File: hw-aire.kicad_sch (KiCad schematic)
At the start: 59 parts, among them J1 Conn_01x02_Pin, J3 Screw_Terminal_01x12, J4 Conn_01x05_Pin, J5 Conn_01x02_Pin, K1 JRC-21F(4100), K2 JRC-21F(4100), K3 JRC-21F(4100), Q1 PMBT3904235, Q2 PMBT3904235, Q3 PMBT3904235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

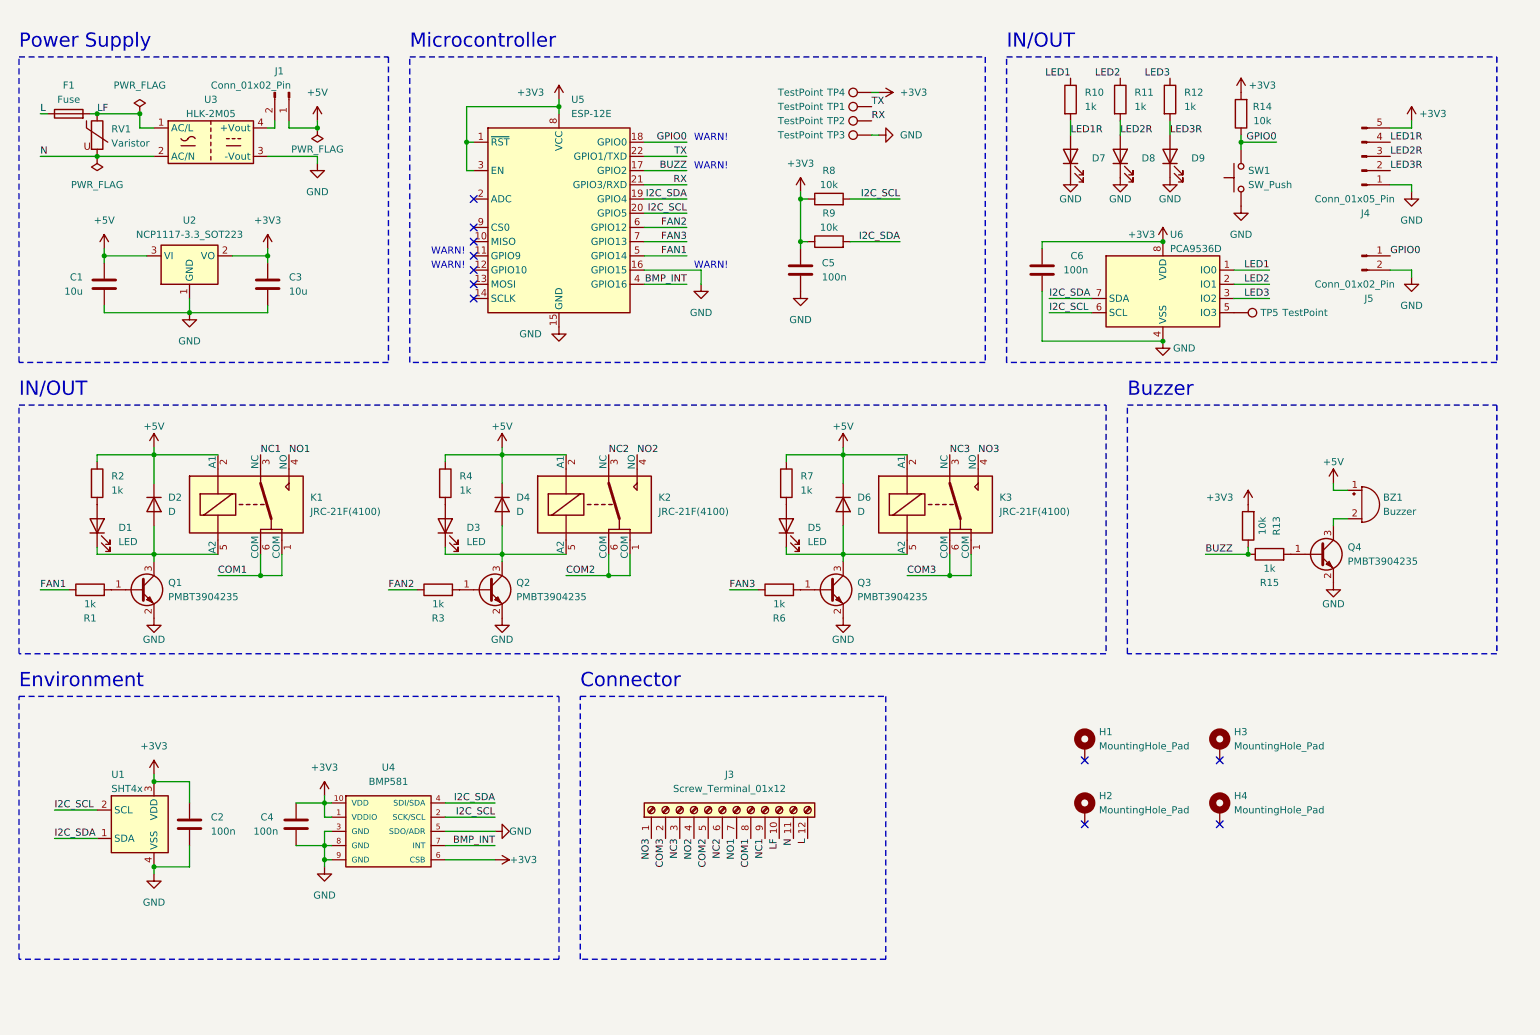
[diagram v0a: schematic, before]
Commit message: Start changing SCH for rev 3.0
- Change ESP8266 to ESP32-SOLO
- Change to cold relays
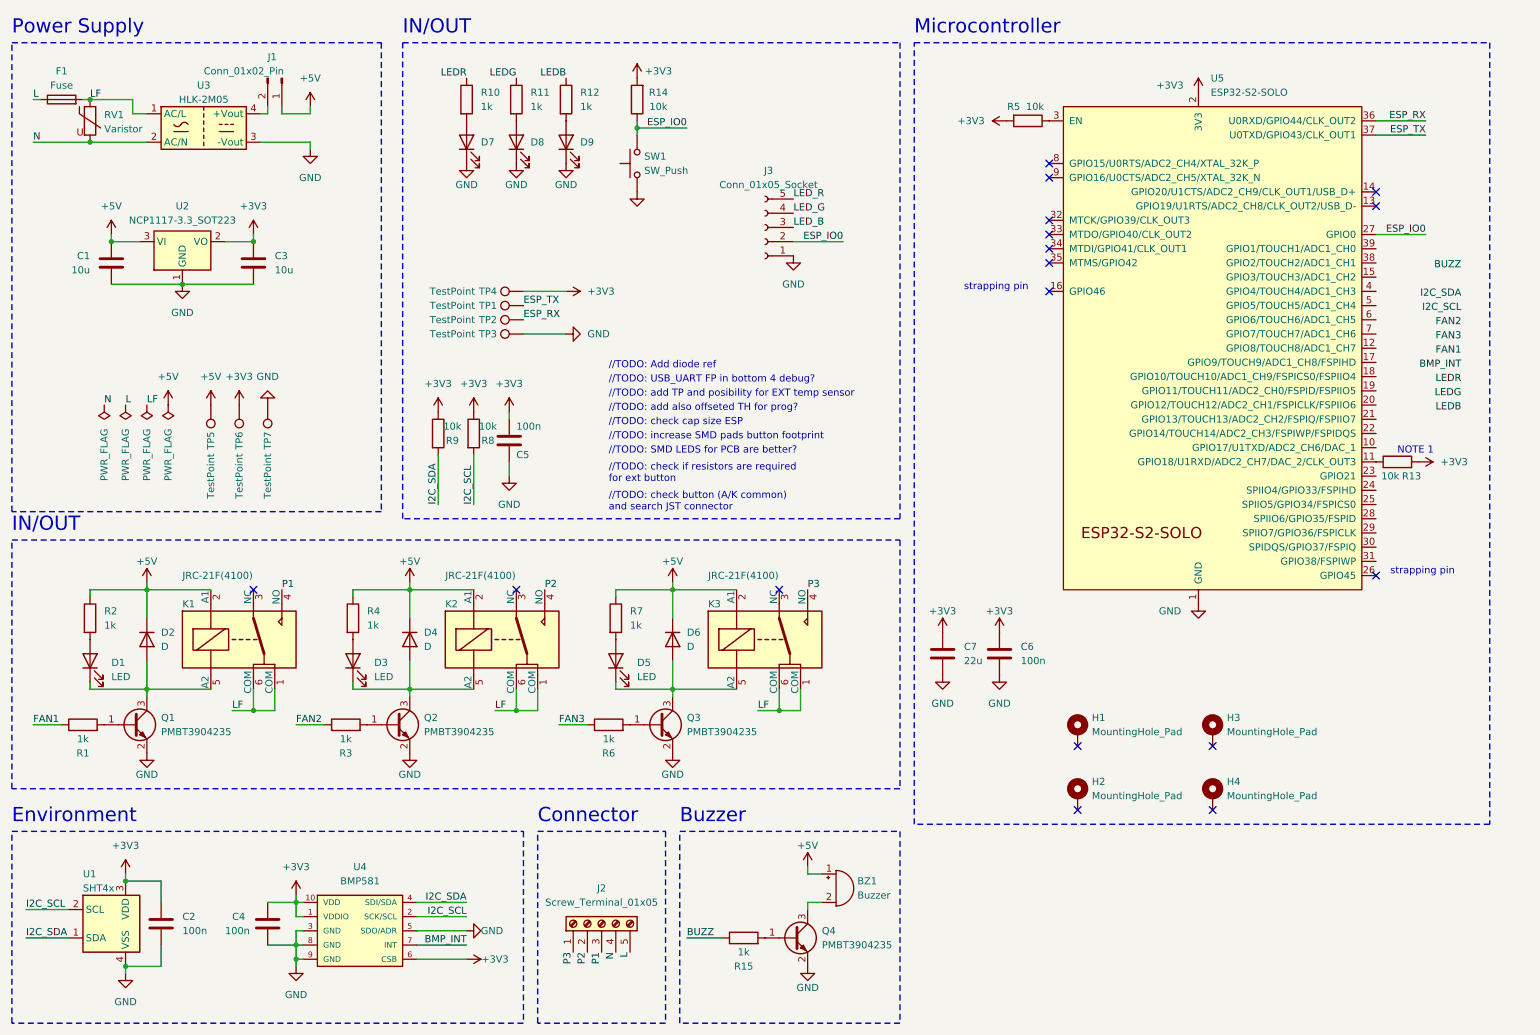
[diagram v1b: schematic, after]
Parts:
- removed J3: Screw_Terminal_01x12, TerminalBlock_Phoenix:TerminalBlock_Phoenix_MKDS-1,5-12-5.08_1x12_P5.08mm_Horizontal, symbol Connector:Screw_Terminal_01x12
- removed J4: Conn_01x05_Pin, Connector_PinHeader_2.54mm:PinHeader_1x05_P2.54mm_Horizontal, symbol Connector:Conn_01x05_Pin
- removed J5: Conn_01x02_Pin, Connector_PinHeader_2.54mm:PinHeader_1x02_P2.54mm_Horizontal, symbol Connector:Conn_01x02_Pin
- removed U5: ESP-12E, RF_Module:ESP-12E, symbol RF_Module:ESP-12E
- removed U6: PCA9536D, Package_SO:SOIC-8_3.9x4.9mm_P1.27mm, symbol Interface_Expansion:PCA9536D
- added C7: 22u, Capacitor_SMD:C_0805_2012Metric, symbol Device:C
- added J2: Screw_Terminal_01x05, symbol Connector:Screw_Terminal_01x05
- added J3: Conn_01x05_Socket, symbol Connector:Conn_01x05_Socket
- added R5: 10k, Resistor_SMD:R_0402_1005Metric, symbol Device:R
- added TP6, TP7: TestPoint, TestPoint:TestPoint_Pad_D1.5mm, symbol Connector:TestPoint
- added U5: ESP32-S2-SOLO, PCM_Espressif:ESP32-S2-SOLO, symbol guille-lib:ESP32-S2-SOLO
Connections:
- net COM1 is gone; now on net LF: K1.1 (COM), K1.6 (COM)
- net COM2 is gone; now on net LF: K2.1 (COM), K2.6 (COM)
- net COM3 is gone; now on net LF: K3.1 (COM), K3.6 (COM)
- net +3V3: now also C7.1, R5.2, TP6.1, U5.2 (3V3)
- net +5V: now also TP5.1
- net BUZZ: no longer R13.1
- net GND: now also C7.2, J3.1 (Pin_1), TP7.1, U5.1 (GND), U5.40 (GND), U5.41 (GND)
- net L: now also J2.5 (Pin_5)
- net N: now also J2.4 (Pin_4)
- net GPIO0 renamed ESP_IO0
- net ESP_IO0: now also J3.2 (Pin_2), U5.27 (GPIO0)
- net LED1 renamed LEDR
- net LED1R: no longer names the net of D7.2 (A), R10.2
- net LED2 renamed LEDG
- net LED2R: no longer names the net of D8.2 (A), R11.2
- net LED3 renamed LEDB
- net LED3R: no longer names the net of D9.2 (A), R12.2
- net NC1: no longer names the net of K1.3 (NC)
- net NC2: no longer names the net of K2.3 (NC)
- net NC3: no longer names the net of K3.3 (NC)
- net NO1 renamed P1
- net P1: now also J2.3 (Pin_3)
- net NO2 renamed P2
- net P2: now also J2.2 (Pin_2)
- net NO3 renamed P3
- net P3: now also J2.1 (Pin_1)
- net RX renamed ESP_RX
- net ESP_RX: now also U5.36 (U0RXD/GPIO44/CLK_OUT2)
- net TX renamed ESP_TX
- net ESP_TX: now also U5.37 (U0TXD/GPIO43/CLK_OUT1)
- new net: R13.1, U5.11 (GPIO18/U1RXD/ADC2_CH7/DAC_2/CLK_OUT3)
- new net: R5.1, U5.3 (EN)
- new net LED_B: J3.3 (Pin_3)
- new net LED_G: J3.4 (Pin_4)
- new net LED_R: J3.5 (Pin_5)
- no-connect marks 11 -> 17
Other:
- note added: "//TODO: Add diode ref"
- note added: "//TODO: SMD LEDS for PCB are better?"
- note added: "//TODO: USB_UART FP in bottom 4 debug?"
- note added: "//TODO: add TP and posibility for EXT temp sensor"
- note added: "//TODO: add also offseted TH for prog?"
- note added: "//TODO: check button (A/K common) and search JST connector"
- note added: "//TODO: check cap size ESP"
- note added: "//TODO: check if resistors are required for ext button"
- note added: "//TODO: increase SMD pads button footprint"
- note added: "NOTE 1"
- note added: "strapping pin"
- note removed: "WARN!"
- moved on the sheet: BZ1, C1, C2, C3, C4, C5, D1, D2, D3, D4, D5, D6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

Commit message: Finish PCB rev 3.0
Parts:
- removed J3: Conn_01x05_Socket, symbol Connector:Conn_01x05_Socket
- added J4: Conn_01x04_Pin, guille-lib:PinHeaderOffset_1x04_P2.54mm_Vertical, symbol Connector:Conn_01x04_Pin
- added J5, J6: Conn_01x06_Socket, Connector_JST:JST_XH_B6B-XH-A_1x06_P2.50mm_Vertical, symbol Connector:Conn_01x06_Socket
- added TP10, TP11, TP12, TP13, TP14, TP15, TP16, TP8, TP9: TestPoint, TestPoint:TestPoint_Pad_D1.5mm, symbol Connector:TestPoint
- D1, D3, D5: footprint LED_SMD:LED_0402_1005Metric -> LED_SMD:LED_0603_1608Metric
- D2, D4, D6: value D -> 1N4448W
- D7, D8, D9: footprint LED_THT:LED_D3.0mm -> LED_SMD:LED_0603_1608Metric
- J2: footprint (none) -> TerminalBlock_Phoenix:TerminalBlock_Phoenix_MKDS-1,5-5-5.08_1x05_P5.08mm_Horizontal
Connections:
- net +3V3: now also J4.1 (Pin_1), J5.6 (Pin_6), J6.5 (Pin_5)
- net +5V: now also J6.6 (Pin_6)
- net BMP_INT: now also U5.22 (GPIO14/TOUCH14/ADC2_CH3/FSPIWP/FSPIDQS)
- net BUZZ: now also U5.12 (GPIO8/TOUCH8/ADC1_CH7)
- net ESP_IO0: now also J5.2 (Pin_2)
- net ESP_RX: now also J4.3 (Pin_3)
- net ESP_TX: now also J4.2 (Pin_2)
- net FAN1: now also U5.18 (GPIO10/TOUCH10/ADC1_CH9/FSPICS0/FSPIIO4)
- net FAN2: now also U5.17 (GPIO9/TOUCH9/ADC1_CH8/FSPIHD)
- net FAN3: now also U5.15 (GPIO3/TOUCH3/ADC1_CH2)
- net GND: now also J4.4 (Pin_4), J5.1 (Pin_1), J6.1 (Pin_1)
- net I2C_SCL: now also U5.4 (GPIO4/TOUCH4/ADC1_CH3)
- net I2C_SDA: now also U5.5 (GPIO5/TOUCH5/ADC1_CH4)
- net LEDB: now also U5.10 (GPIO17/U1TXD/ADC2_CH6/DAC_1), J5.3 (Pin_3)
- net LEDG: now also U5.7 (GPIO7/TOUCH7/ADC1_CH6), J5.4 (Pin_4)
- net LEDR: now also U5.6 (GPIO6/TOUCH6/ADC1_CH5), J5.5 (Pin_5)
- net EXT1: now reaches U5.19 (GPIO11/TOUCH11/ADC2_CH0/FSPID/FSPIIO5)
- net EXT1: now also J6.2 (Pin_2)
- net EXT2: now reaches U5.20 (GPIO12/TOUCH12/ADC2_CH1/FSPICLK/FSPIIO6)
- net EXT2: now also J6.3 (Pin_3)
- net EXT3: now reaches U5.21 (GPIO13/TOUCH13/ADC2_CH2/FSPIQ/FSPIIO7)
- net EXT3: now also J6.4 (Pin_4)
- net at U5.23 (GPIO21): now also TP11.1
- net at U5.24 (SPIIO4/GPIO33/FSPIHD): now also TP8.1
- net at U5.25 (SPIIO5/GPIO34/FSPICS0): now also TP9.1
- net at U5.28 (SPIIO6/GPIO35/FSPID): now also TP10.1
- net at U5.29 (SPIIO7/GPIO36/FSPICLK): now also TP12.1
- net at U5.30 (SPIDQS/GPIO37/FSPIQ): now also TP13.1
- net at U5.31 (GPIO38/FSPIWP): now also TP14.1
- net at U5.38 (GPIO2/TOUCH2/ADC1_CH1): now also TP15.1
- net at U5.39 (GPIO1/TOUCH1/ADC1_CH0): now also TP16.1
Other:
- note added: "I2C MUX?"
- note added: "INTs MUX?"
- note added: "NOTE 1: GPIO18 works as U1RXD and is in floating state when the chip is powered on, which may affect the chip’s entry into download boot mode. To solve this issue, add an external pull-up resistor."
- note added: "Relays"
- note removed: "//TODO: Add diode ref"
- note removed: "//TODO: SMD LEDS for PCB are better?"
- note removed: "//TODO: USB_UART FP in bottom 4 debug?"
- note removed: "//TODO: add TP and posibility for EXT temp sensor"
- note removed: "//TODO: add also offseted TH for prog?"
- note removed: "//TODO: check button (A/K common) and search JST connector"
- note removed: "//TODO: check cap size ESP"
- note removed: "//TODO: check if resistors are required for ext button"
- note removed: "//TODO: increase SMD pads button footprint"
- note removed: "Connector"
- moved on the sheet: BZ1, C1, C2, C3, C4, C5, C6, C7, D1, D2, D3, D4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
